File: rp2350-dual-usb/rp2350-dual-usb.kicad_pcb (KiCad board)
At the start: 4 copper layers, 51 x 32 mm, 53 parts, among them J1 Conn_01x03_MountingPin, J2 USB_C_Receptacle_USB2.0_16P, J3 USB_C_Receptacle_USB2.0_14P, J4 TRS, J5 TRS, SW1 Button_Switch_SMD_Push_1P1T_W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, U1 LDL1117-3.3, U2 RP2354_60QFN, U3 USBLC6-2SC6, U4 USBLC6-2SC6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

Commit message: Updates YouMe Transformer to v1.1, fixing incorrect R10 value. Improves the consistency of the Lichen symbol library.
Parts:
- C1, C11, C6: value 100nF_0402_50V -> 100nF
- C10, C3, C7, C9: value 4.7uF_0402 -> 4.7uF
- C12, C13, C14, C15, C17, C18, C19: value 100nF_0402_16V -> 100nF
- C16: value 100nF_0603_16V -> 100nF
- C2: value 1uF_0805_50V -> 1uF
- C4, C5: value 15pF_0402 -> 15pF
- C8: value 4.7uF_0805_25V -> 4.7uF
- R10: value 7k7_0603 -> 4.7K
- R11: value 33R_0402 -> 33R
- R12: value 10R_0402 -> 10R
- R13, R14: value 220R_0402 -> 220R
- R15: value 470R_0402 -> 470R
- R16, R5, R6: value 1k_0402 -> 1K
- R2: value 1k_0402 -> 1k
- R3: value 27R_0402 -> 27R
- R4: value 33R_0402 -> 27R
- R7, R8: value 5k1_0603 -> 5.1K
- R9: value 4k7_0603 -> 4.7K
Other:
- board text added: "v1.1, January 2026"
- board text removed: "v1.0, December 2025"

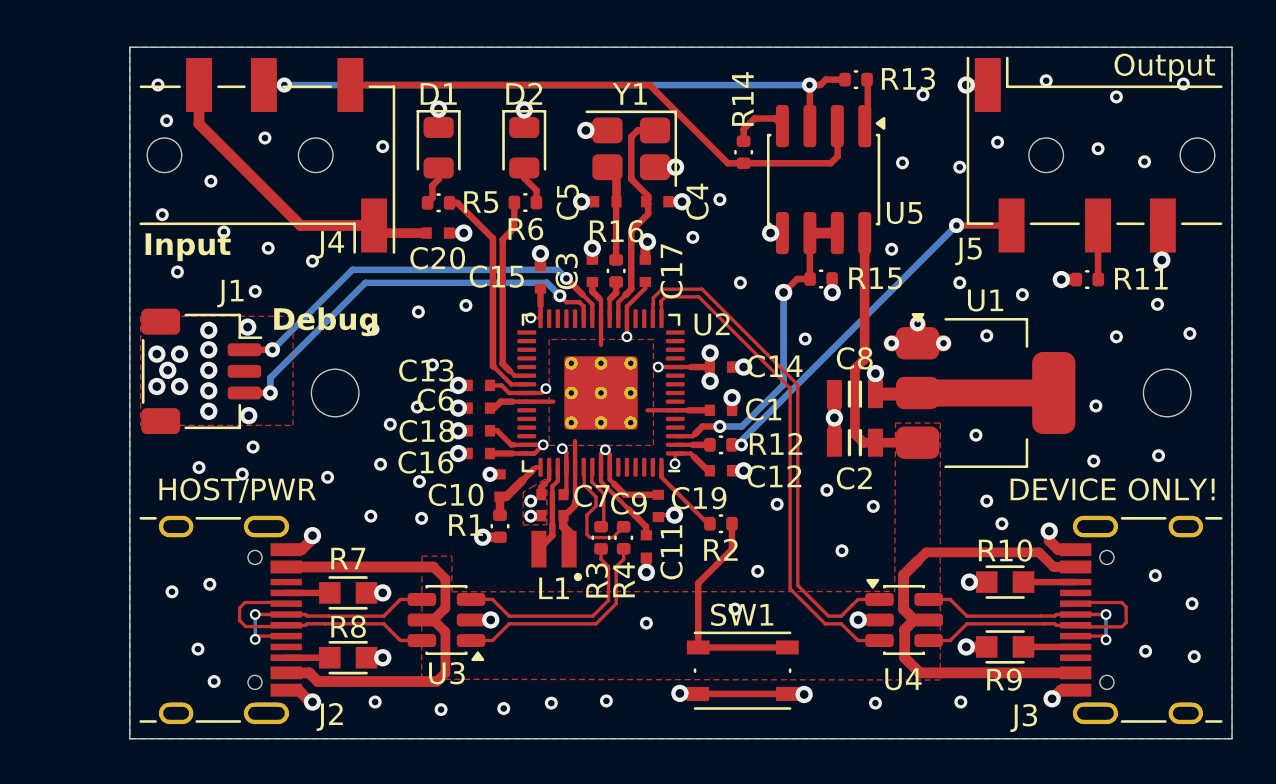
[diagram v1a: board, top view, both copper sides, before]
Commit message: feat: Updates symbol libraries and design blocks. Adds in-progress RP2350-based module.
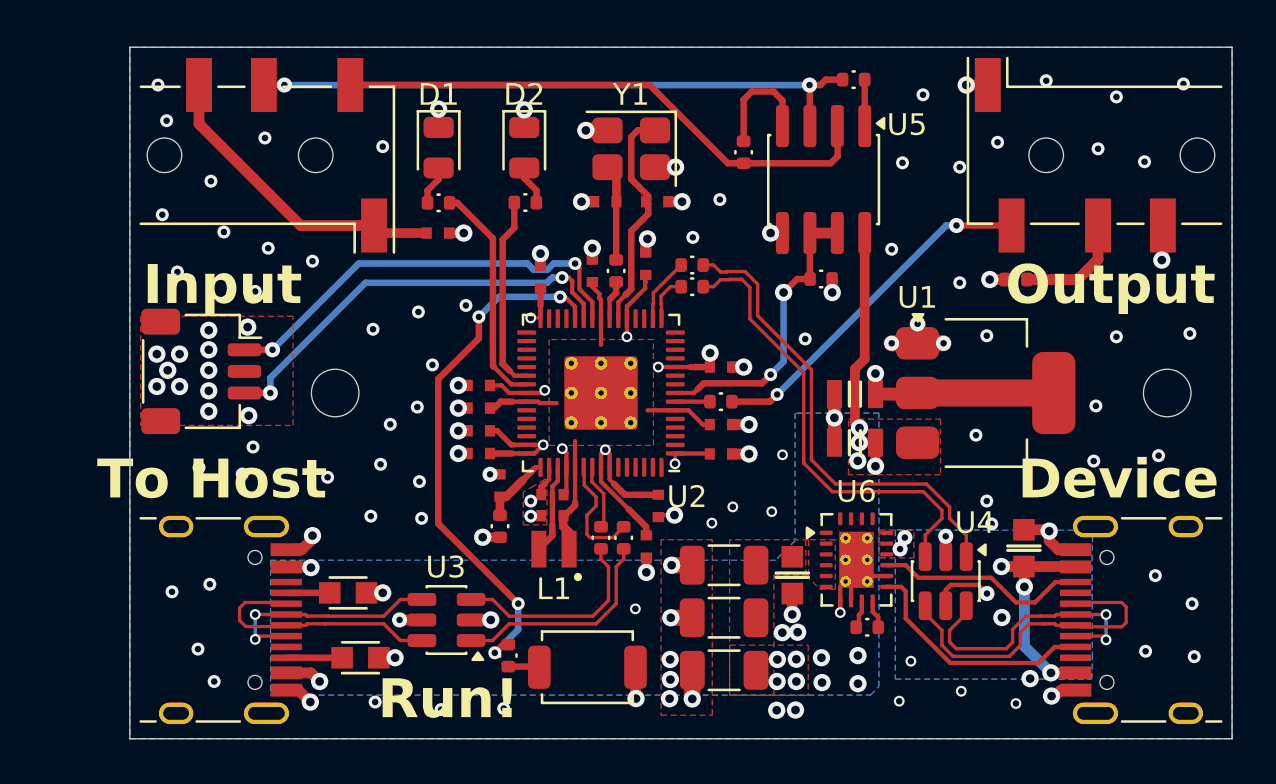
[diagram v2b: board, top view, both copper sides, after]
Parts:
- removed R10, R9: 4.7K, Lichen:R_0603
- added C21: 100nF, Lichen:C_0603, F.Cu at (130.7, 124.4)
- added C22: 10uF, Lichen:C_0603, F.Cu at (141.4, 123.2)
- added C23: 47uF, Capacitor_SMD:C_1206_3216Metric, F.Cu at (127.5, 128.8)
- added C24: 47uF, Capacitor_SMD:C_1206_3216Metric, F.Cu at (127.5, 124.0)
- added C25: 47uF, Capacitor_SMD:C_1206_3216Metric, F.Cu at (127.5, 126.4)
- added R17: 27R, Lichen:R_0402_1005Metric, F.Cu at (126.0, 111.1)
- added R18: 27R, Lichen:R_0402_1005Metric, F.Cu at (126.0, 110.1)
- added R19: 100K, Lichen:R_0402_1005Metric, F.Cu at (134.1, 126.8)
- added U6: TPS25810RVC, Lichen:Texas_RVC0020A_WQFN-20-1EP_3x4mm_P0.5mm_EP1.6x2.6mm_ThermalVias, F.Cu at (133.6, 123.7)
- R6: value 1K -> 1.5K
- SW1: footprint Lichen:SW_Push_1P1T_NO_Vertical_Wuerth_434133025816 -> Button_Switch_SMD:SW_SPST_TS-1088-xR020
- moved R2 11.6 mm to (117.5, 128.2), turned to 90 degrees
- moved SW1 7.18 mm to (121.2, 128.7)
- moved R11 3.30 mm to (141.0, 110.8)
- moved U4 2.63 mm to (137.8, 124.7), turned to -90 degrees
- moved R12 2.00 mm to (127.3, 116.4)
- moved C12 0.78 mm to (127.3, 118.8)
- moved C1 0.66 mm to (127.3, 117.5)
- moved R8 0.57 mm to (110.7, 128.2)
- moved C17 0.33 mm to (123.9, 110.0)
- moved R13 0.11 mm to (133.5, 101.5)
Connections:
- J3 pad A4: VBUS -> /Connectors/HOST_VBUS_OUT
- J3 pad A5: /Connectors/USB2.CC1 -> Net-(J3-CC1)
- J3 pad A9: VBUS -> /Connectors/HOST_VBUS_OUT
- J3 pad B4: VBUS -> /Connectors/HOST_VBUS_OUT
- J3 pad B5: /Connectors/USB2.CC2 -> Net-(J3-CC2)
- J3 pad B9: VBUS -> /Connectors/HOST_VBUS_OUT
- R2 pad 2: Net-(U2-QSPI_SS) -> Net-(U2-RUN)
- U2 pad 16: USB2_ESD.D+ -> /USB2.D+
- U2 pad 17: USB2_ESD.D- -> /USB2.D-
- U2 pad 2: MIDI_OUT_UART_TX -> unconnected-(U2-GPIO0-Pad2)
- U2 pad 26: unconnected-(U2-RUN-Pad26) -> Net-(U2-RUN)
- U2 pad 3: MIDI_IN_UART_RX -> unconnected-(U2-GPIO1-Pad3)
- U2 pad 60: Net-(U2-QSPI_SS) -> unconnected-(U2-QSPI_SS-Pad60)
- U2 pad 7: unconnected-(U2-GPIO4-Pad7) -> MIDI_OUT_UART_TX
- U2 pad 8: unconnected-(U2-GPIO5-Pad8) -> MIDI_IN_UART_RX
- U4 pad 5: VBUS -> /Connectors/HOST_VBUS_OUT
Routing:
- net VBUS: track 55.0 -> 15.0 mm, vias 0 -> 11
- net Net-(U2-RUN): track 0.00 -> 24.7 mm, vias 0 -> 4
- net /Connectors/HOST_VBUS_OUT: track 0.00 -> 12.9 mm, vias 0 -> 6
- net Net-(J3-CC1): track 0.00 -> 11.2 mm
- net Net-(J3-CC2): track 0.00 -> 9.85 mm
- net Net-(R2-Pad1): track 10.5 -> 1.40 mm
- net GND: track 38.4 -> 44.3 mm, vias 124 -> 136
- net Net-(U2-QSPI_SS): track 3.64 -> 0.00 mm
- net /USB2.D-: track 0.00 -> 3.03 mm
- net Net-(J5-PadR): track 2.50 -> 5.24 mm
- net /Connectors/USB2.CC1: track 2.61 -> 0.00 mm
- net Net-(U5-A2): track 2.70 -> 5.23 mm
- net +3V3: track 43.8 -> 41.3 mm, vias 16 -> 13
- net /Connectors/USB2.CC2: track 2.41 -> 0.00 mm
- net /Connectors/USB2_CONN.D+: track 12.8 -> 15.2 mm
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- added copper zone on B.Cu, net /Connectors/HOST_VBUS_OUT
- added copper zone on F.Cu, net /Connectors/HOST_VBUS_OUT
- added copper zone on B.Cu, net VBUS
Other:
- board text added: "Device"
- board text added: "LPZW auto-crossover MIDI input circuit by Kay Knofe"
- board text added: "Run!"
- board text added: "To Host"
- board text added: "v1.2, February 2026"
- board text removed: "(Thanks to Kay Knofe for the LPZW auto-crossover MIDI input)"
- board text removed: "DEVICE ONLY!"
- board text removed: "Debug"
- board text removed: "HOST/PWR"
- board text removed: "v1.1, January 2026"
